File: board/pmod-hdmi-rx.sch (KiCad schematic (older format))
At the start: 15 parts, among them P1 PMOD-CONN_6X2, U31 XC9140, U32 REG710-DBV

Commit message: Rewriting for RX.
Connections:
- net HDMI_TX0_CLK+ renamed HDMI_RX0_CLK+
- net HDMI_TX0_CLK- renamed HDMI_RX0_CLK-
- net HDMI_TX0_D0+ renamed HDMI_RX0_D0+
- net HDMI_TX0_D0- renamed HDMI_RX0_D0-
- net HDMI_TX0_D1+ renamed HDMI_RX0_D1+
- net HDMI_TX0_D1- renamed HDMI_RX0_D1-
- net HDMI_TX0_D2+ renamed HDMI_RX0_D2+
- net HDMI_TX0_D2- renamed HDMI_RX0_D2-
- net HDMI_TX0_DCC_EN renamed HDMI_RX0_DCC_EN
- net HDMI_TX0_DDET renamed HDMI_RX0_DDET
- net HDMI_TX0_EQ0 renamed HDMI_RX0_EQ0
- net HDMI_TX0_EQ1 renamed HDMI_RX0_EQ1
- net TX05V0 renamed RX05V0
- net ~HDMI_TX0_OE renamed ~HDMI_RX0_OE
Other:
- note added: "On PRX0\n - DET on Pin X\n - DDC on Pin X\n - EQ1 on Pin X\n - EQ0 on Pin X"
- note added: "On PRX0\n - SCL on Pin X\n - SDA on Pin X\n - CEC on Pin X\n - HPD on Pin X"
- note removed: "On PTX0\n - DET on Pin X\n - DDC on Pin X\n - EQ1 on Pin X\n - EQ0 on Pin X"
- note removed: "On PTX0\n - SCL on Pin X\n - SDA on Pin X\n - CEC on Pin X\n - HPD on Pin X"
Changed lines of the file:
@@
 LIBS:xc9140
 LIBS:reg710-dbv
-LIBS:pmod-hdmi-tx-cache
+LIBS:pmod-hdmi-rx-cache
 EELAYER 25 0
 EELAYER END
@@
 Date ""
 Rev ""
-Comp "https://github.com/mithro/pmod-hdmi-tx-ptn3363"
-Comment1 "Using references from Numato Lab and Apertus AXIOM"
+Comp "https://github.com/mithro/pmod-hdmi-rx-ad8195"
+Comment1 ""
 Comment2 "Designed by TimVideos.us"
 Comment3 "License: CC-BY-SA 4.0 International"
@@
 S 4150 1400 2100 1600
 U 5802F547
-F0 "HDMI TX" 60
-F1 "hdmi_TX0.sch" 60
-F2 "~HDMI_TX0_OE" I R 6250 2000 60
-F3 "HDMI_TX0_EQ0" I R 6250 2600 60
-F4 "HDMI_TX0_EQ1" I R 6250 2500 60
-F5 "HDMI_TX0_DDC_EN" I R 6250 2350 60
-F6 "HDMI_TX0_CLK+" I L 4150 2250 60
-F7 "HDMI_TX0_CLK-" I L 4150 2350 60
-F8 "HDMI_TX0_D0+" I L 4150 2000 60
-F9 "HDMI_TX0_D0-" I L 4150 2100 60
-F10 "HDMI_TX0_D1+" I L 4150 1750 60
-F11 "HDMI_TX0_D1-" I L 4150 1850 60
-F12 "HDMI_TX0_D2+" I L 4150 1500 60
-F13 "HDMI_TX0_D2-" I L 4150 1600 60
-F14 "HDMI_TX0_SCL" B R 6250 1500 60
-F15 "HDMI_TX0_SDA" B R 6250 1600 60
-F16 "HDMI_TX0_DDET" I R 6250 2250 60
-F17 "HDMI_TX0_HPD" O R 6250 1800 60
-F18 "HDMI_TX0_HIZ_EN" I R 6250 2100 60
-F19 "HDMI_TX0_CEC" I R 6250 1700 60
+F0 "HDMI RX" 60
+F1 "hdmi_RX0.sch" 60
+F2 "~HDMI_RX0_OE" I R 6250 2000 60
+F3 "HDMI_RX0_EQ0" I R 6250 2600 60
+F4 "HDMI_RX0_EQ1" I R 6250 2500 60
+F5 "HDMI_RX0_DDC_EN" I R 6250 2350 60
+F6 "HDMI_RX0_CLK+" I L 4150 2250 60
+F7 "HDMI_RX0_CLK-" I L 4150 2350 60
+F8 "HDMI_RX0_D0+" I L 4150 2000 60
+F9 "HDMI_RX0_D0-" I L 4150 2100 60
+F10 "HDMI_RX0_D1+" I L 4150 1750 60
+F11 "HDMI_RX0_D1-" I L 4150 1850 60
+F12 "HDMI_RX0_D2+" I L 4150 1500 60
+F13 "HDMI_RX0_D2-" I L 4150 1600 60
+F14 "HDMI_RX0_SCL" B R 6250 1500 60
+F15 "HDMI_RX0_SDA" B R 6250 1600 60
+F16 "HDMI_RX0_DDET" I R 6250 2250 60
+F17 "HDMI_RX0_HPD" O R 6250 1800 60
+F18 "HDMI_RX0_HIZ_EN" I R 6250 2100 60
+F19 "HDMI_RX0_CEC" I R 6250 1700 60
 $EndSheet
 Text Label 3300 3000 0    60   ~ 0
-HDMI_TX0_CLK-
+HDMI_RX0_CLK-
 Text Label 3300 2900 0    60   ~ 0
-HDMI_TX0_D0-
+HDMI_RX0_D0-
 Text Label 3300 2800 0    60   ~ 0
-HDMI_TX0_D1-
+HDMI_RX0_D1-
 Text Label 3300 2700 0    60   ~ 0
-HDMI_TX0_D2-
+HDMI_RX0_D2-
 Text Label 1700 2700 2    60   ~ 0
-HDMI_TX0_D2+
+HDMI_RX0_D2+
 Text Label 1700 2800 2    60   ~ 0
-HDMI_TX0_D1+
+HDMI_RX0_D1+
 Text Label 1700 2900 2    60   ~ 0
-HDMI_TX0_D0+
+HDMI_RX0_D0+
 Text Label 1700 3000 2    60   ~ 0
-HDMI_TX0_CLK+
+HDMI_RX0_CLK+
 $Comp
 L GND #PWR01
@@
 $EndComp
 Text GLabel 3550 6000 2    60   Input ~ 0
-TX05V0
+RX05V0
 Text GLabel 5250 1125 2    60   Input ~ 0
 VCC3V3
 Text Label 3550 6075 3    60   ~ 0
-TX05V0
+RX05V0
 $Comp
 L GND #PWR05
@@
 Option 1\n
 Text Label 8125 1500 0    60   ~ 0
-HDMI_TX0_SCL
+HDMI_RX0_SCL
 Text Label 8125 1600 0    60   ~ 0
-HDMI_TX0_SDA
+HDMI_RX0_SDA
 Text Label 8125 1700 0    60   ~ 0
-HDMI_TX0_CEC
+HDMI_RX0_CEC
 Text Label 8125 1800 0    60   ~ 0
-HDMI_TX0_HPD
+HDMI_RX0_HPD
 Text Notes 8875 1850 0    60   ~ 0
-On PTX0\n - SCL on Pin X\n - SDA on Pin X\n - CEC on Pin X\n - HPD on Pin X
+On PRX0\n - SCL on Pin X\n - SDA on Pin X\n - CEC on Pin X\n - HPD on Pin X
 Text Notes 1850 4200 0    60   ~ 0
 HDMI High Speed Signals\nPositive signals on Top Row\nNegative signals on Bottom Row
@@
 $EndComp
 Text Label 7975 2500 0    60   ~ 0
-HDMI_TX0_EQ1
+HDMI_RX0_EQ1
 Text Label 7975 2600 0    60   ~ 0
-HDMI_TX0_EQ0
+HDMI_RX0_EQ0
 Text Notes 8875 2600 0    60   ~ 0
-On PTX0\n - DET on Pin X\n - DDC on Pin X\n - EQ1 on Pin X\n - EQ0 on Pin X
+On PRX0\n - DET on Pin X\n - DDC on Pin X\n - EQ1 on Pin X\n - EQ0 on Pin X
 Text Label 7975 2250 0    60   ~ 0
-HDMI_TX0_DDET
+HDMI_RX0_DDET
 Text Label 7975 2350 0    60   ~ 0
-HDMI_TX0_DCC_EN
+HDMI_RX0_DCC_EN
 Text Label 6300 2000 0    60   ~ 0
-~HDMI_TX0_OE
+~HDMI_RX0_OE
 Text Label 6300 2100 0    60   ~ 0
-HDMI_TX0_HIZ_EN
+HDMI_RX0_HIZ_EN
 $Comp
 L R RDE1

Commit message: Getting RX wired up.
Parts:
- removed ROE1: 10k, Resistors_SMD:R_0402, symbol R
- added D0, D1: LED, symbol LED
- added PE1: CONN_02X02, symbol CONN_02X02
- added PWP1: CONN_02X01, symbol CONN_02X01
- added RWP1: 10k, symbol R
- added UE1: 24AA01/24LC01B, symbol 24AA01/24LC01B
- RD0: renamed from REQ1; value 10k -> 100
- RD1: renamed from REQ0; value 10k -> 100
- renumbered RDC1 to RPE1, RDE1 to RTX1
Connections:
- net GND: now also RWP1.2, UE1.2 (VSS); no longer RPE1.1, RTX1.1
- net HDMI_RX0_SCL: now also PE1.1 (P1)
- net HDMI_RX0_SDA: now also PE1.3 (P3)
- net VCC: now also RPE1.1, RTX1.1, D0.2 (A), D1.2 (A), PWP1.2 (P2), UE1.4 (VCC); no longer RD0.1, RD1.1
- net HDMI_RX0_DCC_EN renamed HDMI_RX0_PEEN
- net HDMI_RX0_DDET renamed HDMI_RX0_TXEN
- net HDMI_RX0_EQ0 renamed HDMI_RX0_IO1
- net HDMI_RX0_EQ1 renamed HDMI_RX0_IO0
- net RX05V0 renamed VCC5V0
- new net: PWP1.1 (P1), RWP1.1, UE1.5 (WP)
- new net: D0.1 (K), RD0.1
- new net: D1.1 (K), RD1.1
- new net EEPROM_SCL: PE1.2 (P2), UE1.1 (SCL)
- new net EEPROM_SDA: PE1.4 (P4), UE1.3 (SDA)
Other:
- note added: "Jumpering PW1 will cause the \nEEPROM to be read only."
- note added: "On PRX0\n - TXEN on Pin X\n - PEEN on Pin X\n - IO0 on Pin X\n - IO1 on Pin X"
- note added: "TXEN is pulled high (1) by default, enabling receive.\nPEEN is pulled high (1) by default, enabling 6dB preemphasis."
- note removed: "By default, EQ0 and EQ1\nare pulled to VCC\ngiving 6dB equalization"
- note removed: "On PRX0\n - DET on Pin X\n - DDC on Pin X\n - EQ1 on Pin X\n - EQ0 on Pin X"

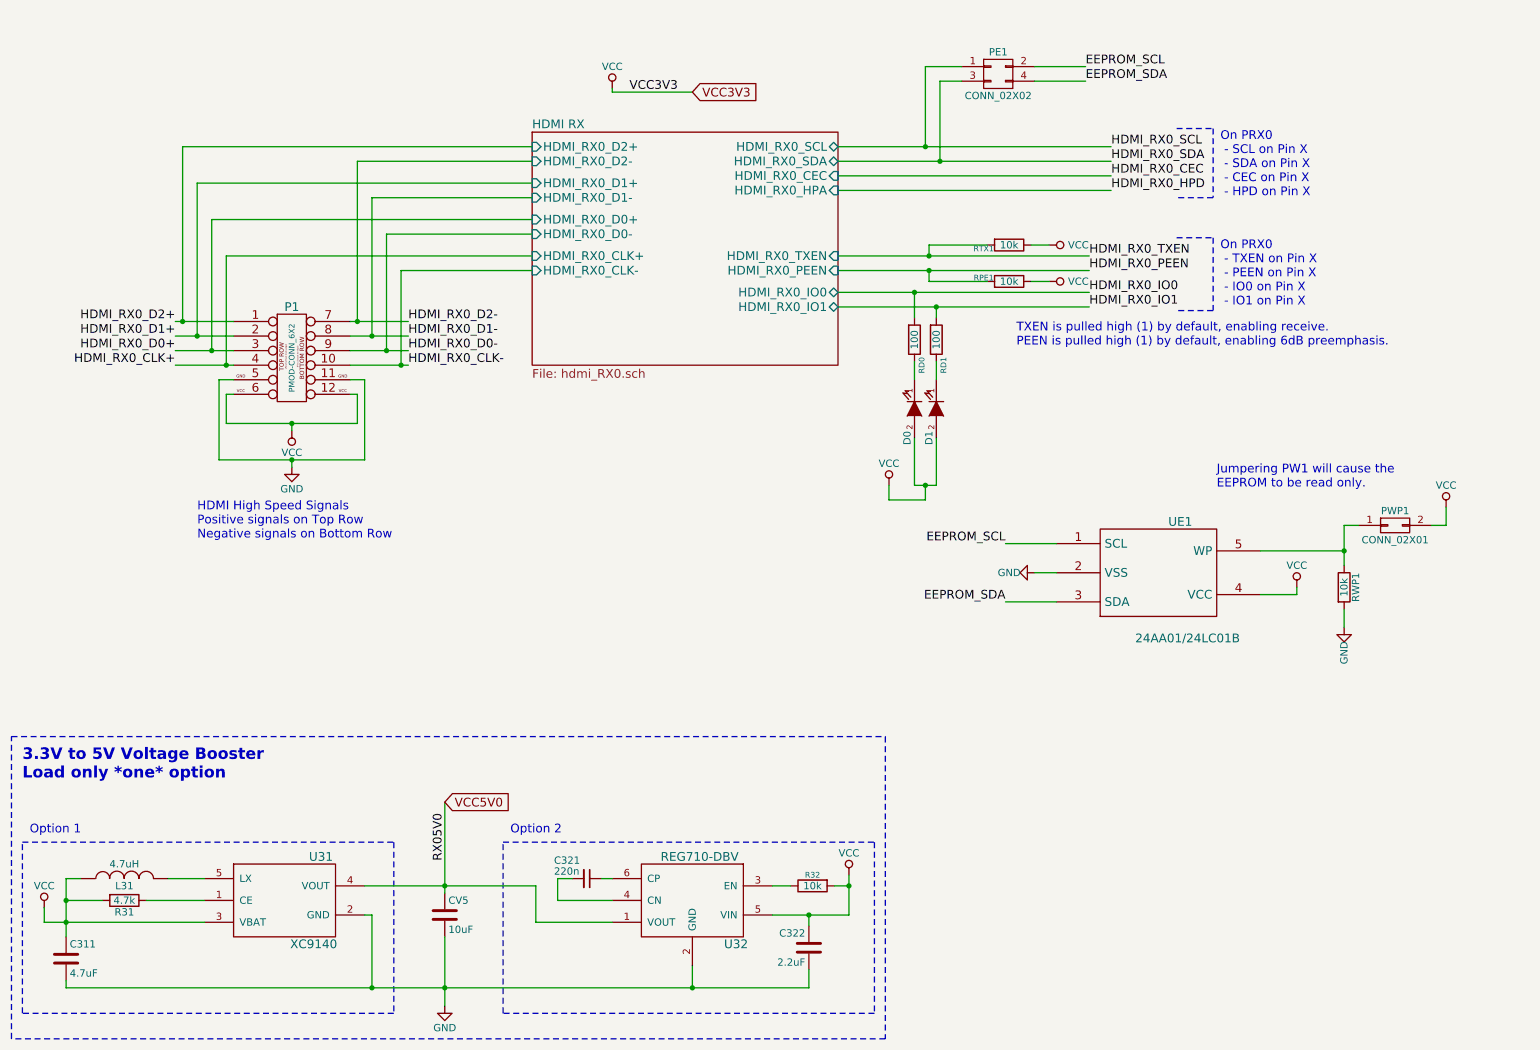
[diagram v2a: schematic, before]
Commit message: Slowly getting the RX version working.
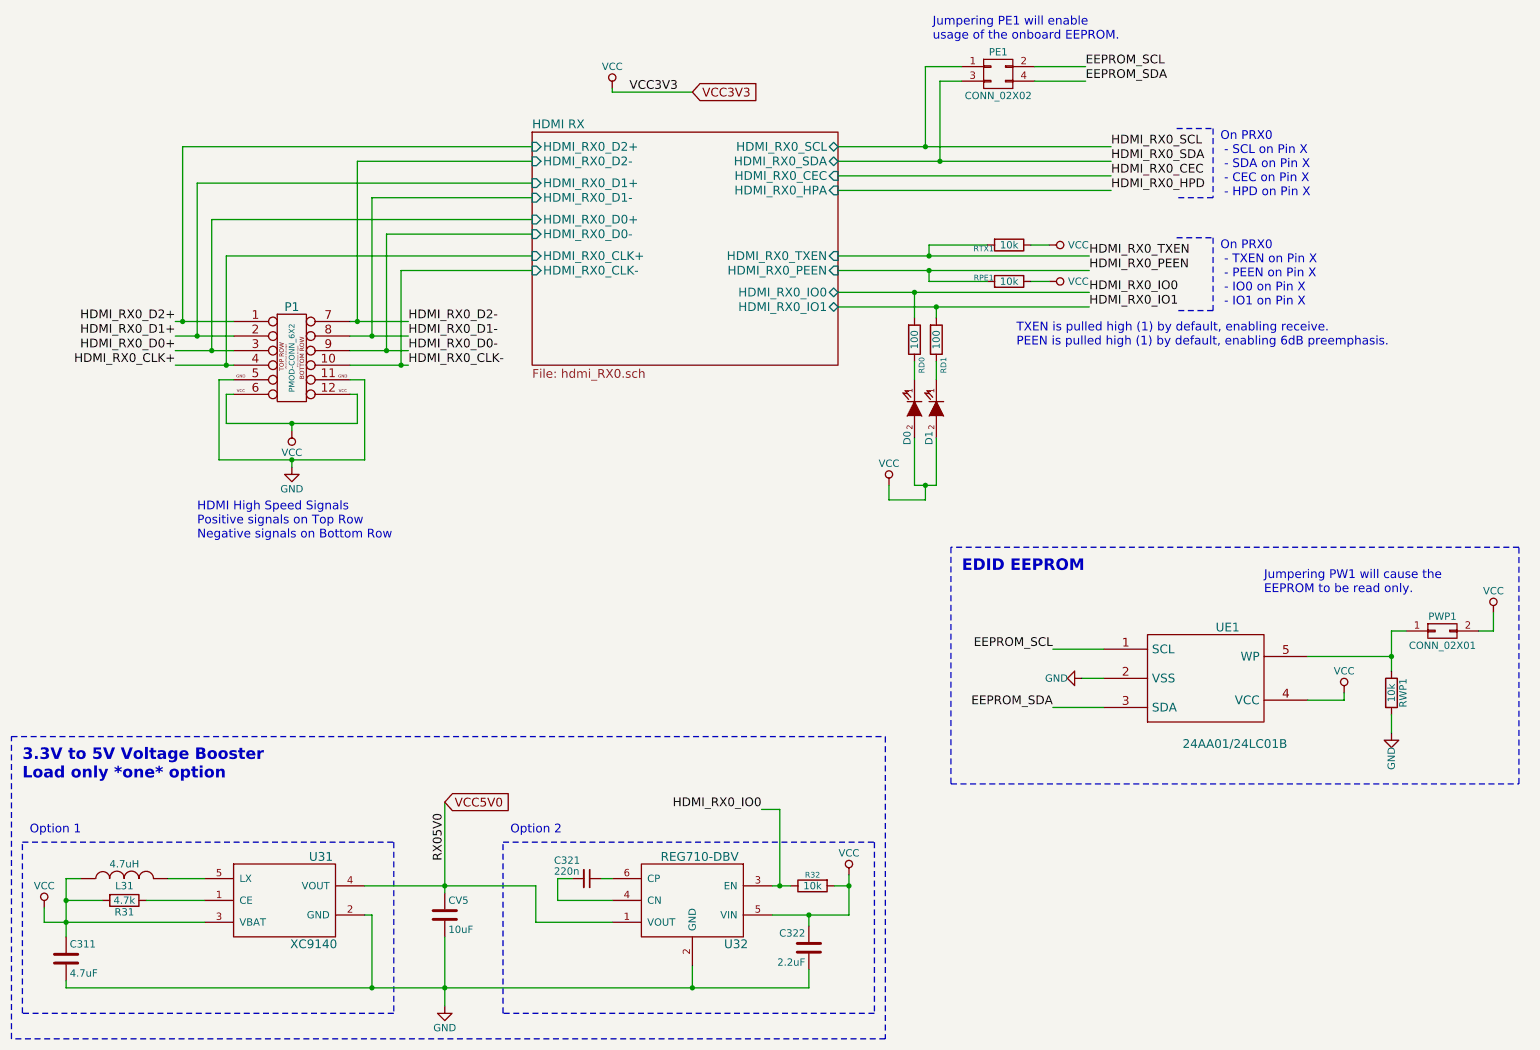
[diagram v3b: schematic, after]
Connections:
- net HDMI_RX0_IO0: now also R32.1, U32.3 (EN)
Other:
- note added: "EDID EEPROM"
- note added: "Jumpering PE1 will enable\nusage of the onboard EEPROM."
- moved on the sheet: PWP1, RWP1, UE1
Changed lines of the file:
@@
 LIBS:pmod
 LIBS:hdmi
-LIBS:ptn3363
 LIBS:ma78l00
 LIBS:pmod-conn_6x2
@@
 LIBS:xc9140
 LIBS:reg710-dbv
+LIBS:ad8195
+LIBS:fdv301n
 LIBS:pmod-hdmi-rx-cache
 EELAYER 25 0
@@
 L VCC #PWR08
 U 1 1 58039EF2
-P 9400 4525
-F 0 "#PWR08" H 9400 4375 50  0001 C CNN
-F 1 "VCC" H 9400 4675 50  0000 C CNN
-F 2 "" H 9400 4525 50  0000 C CNN
-F 3 "" H 9400 4525 50  0000 C CNN
-	1    9400 4525
+P 9725 5250
+F 0 "#PWR08" H 9725 5100 50  0001 C CNN
+F 1 "VCC" H 9725 5400 50  0000 C CNN
+F 2 "" H 9725 5250 50  0000 C CNN
+F 3 "" H 9725 5250 50  0000 C CNN
+	1    9725 5250
 	1    0    0    -1
 $EndComp
@@
 	2900 3100 3000 3100
 Wire Wire Line
-	3000 3650 3000 3100
-Wire Wire Line
-	2000 3650 3000 3650
+	3000 3100 3000 3650
+Wire Wire Line
+	3000 3650 2000 3650
 Wire Wire Line
 	2000 3650 2000 3100
@@
 L 24AA01/24LC01B UE1
 U 1 1 58037E0C
-P 8450 4425
-F 0 "UE1" H 8600 4775 60  0000 C CNN
-F 1 "24AA01/24LC01B" H 8650 3975 60  0000 C CNN
-F 2 "" H 8450 4425 60  0000 C CNN
-F 3 "" H 8450 4425 60  0000 C CNN
-	1    8450 4425
-	1    0    0    -1
-$EndComp
-Wire Wire Line
-	7750 4225 7400 4225
-Wire Wire Line
-	7750 4625 7400 4625
-Text Label 7400 4225 2    60   ~ 0
+P 8775 5150
+F 0 "UE1" H 8925 5500 60  0000 C CNN
+F 1 "24AA01/24LC01B" H 8975 4700 60  0000 C CNN
+F 2 "" H 8775 5150 60  0000 C CNN
+F 3 "" H 8775 5150 60  0000 C CNN
+	1    8775 5150
+	1    0    0    -1
+$EndComp
+Wire Wire Line
+	8075 4950 7725 4950
+Wire Wire Line
+	8075 5350 7725 5350
+Text Label 7725 4950 2    60   ~ 0
 EEPROM_SCL
-Text Label 7400 4625 2    60   ~ 0
+Text Label 7725 5350 2    60   ~ 0
 EEPROM_SDA
 $Comp
 L GND #PWR?
 U 1 1 5803B7CA
-P 7600 4425
-F 0 "#PWR?" H 7600 4175 50  0001 C CNN
-F 1 "GND" V 7600 4250 50  0000 C CNN
-F 2 "" H 7600 4425 50  0000 C CNN
-F 3 "" H 7600 4425 50  0000 C CNN
-	1    7600 4425
+P 7925 5150
+F 0 "#PWR?" H 7925 4900 50  0001 C CNN
+F 1 "GND" V 7925 4975 50  0000 C CNN
+F 2 "" H 7925 5150 50  0000 C CNN
+F 3 "" H 7925 5150 50  0000 C CNN
+	1    7925 5150
 	0    1    -1   0
 $EndComp
 Wire Wire Line
-	7750 4425 7600 4425
-Wire Wire Line
-	9400 4525 9400 4575
-Wire Wire Line
-	9400 4575 9150 4575
-Wire Wire Line
-	9150 4275 9725 4275
+	8075 5150 7925 5150
+Wire Wire Line
+	9725 5250 9725 5300
+Wire Wire Line
+	9725 5300 9475 5300
+Wire Wire Line
+	9475 5000 10050 5000
 $Comp
 L R RWP1
 U 1 1 5803C11E
-P 9725 4525
-F 0 "RWP1" V 9805 4525 50  0000 C CNN
-F 1 "10k" V 9725 4525 50  0000 C CNN
-F 2 "" V 9655 4525 50  0000 C CNN
-F 3 "" H 9725 4525 50  0000 C CNN
-	1    9725 4525
-	1    0    0    -1
-$EndComp
-Wire Wire Line
-	9725 4100 9725 4375
-Wire Wire Line
-	9725 4675 9725 4800
+P 10050 5250
+F 0 "RWP1" V 10130 5250 50  0000 C CNN
+F 1 "10k" V 10050 5250 50  0000 C CNN
+F 2 "" V 9980 5250 50  0000 C CNN
+F 3 "" H 10050 5250 50  0000 C CNN
+	1    10050 5250
+	1    0    0    -1
+$EndComp
+Wire Wire Line
+	10050 4825 10050 5100
+Wire Wire Line
+	10050 5400 10050 5525
 $Comp
 L GND #PWR?
 U 1 1 5803C747
-P 9725 4800
-F 0 "#PWR?" H 9725 4550 50  0001 C CNN
-F 1 "GND" V 9725 4625 50  0000 C CNN
-F 2 "" H 9725 4800 50  0000 C CNN
-F 3 "" H 9725 4800 50  0000 C CNN
-	1    9725 4800
+P 10050 5525
+F 0 "#PWR?" H 10050 5275 50  0001 C CNN
+F 1 "GND" V 10050 5350 50  0000 C CNN
+F 2 "" H 10050 5525 50  0000 C CNN
+F 3 "" H 10050 5525 50  0000 C CNN
+	1    10050 5525
 	-1   0    0    -1
 $EndComp
@@
 L CONN_02X01 PWP1
 U 1 1 5803C8DA
-P 10075 4100
-F 0 "PWP1" H 10075 4200 50  0000 C CNN
-F 1 "CONN_02X01" H 10075 4000 50  0000 C CNN
-F 2 "" H 10075 2900 50  0000 C CNN
-F 3 "" H 10075 2900 50  0000 C CNN
-	1    10075 4100
-	1    0    0    -1
-$EndComp
-Wire Wire Line
-	9725 4100 9825 4100
-Connection ~ 9725 4275
-Wire Wire Line
-	10325 4100 10425 4100
-Wire Wire Line
-	10425 4100 10425 3975
+P 10400 4825
+F 0 "PWP1" H 10400 4925 50  0000 C CNN
+F 1 "CONN_02X01" H 10400 4725 50  0000 C CNN
+F 2 "" H 10400 3625 50  0000 C CNN
+F 3 "" H 10400 3625 50  0000 C CNN
+	1    10400 4825
+	1    0    0    -1
+$EndComp
+Wire Wire Line
+	10050 4825 10150 4825
+Connection ~ 10050 5000
+Wire Wire Line
+	10650 4825 10750 4825
+Wire Wire Line
+	10750 4825 10750 4700
 $Comp
 L VCC #PWR?
 U 1 1 5803CDCA
-P 10425 3975
-F 0 "#PWR?" H 10425 3825 50  0001 C CNN
-F 1 "VCC" H 10425 4125 50  0000 C CNN
-F 2 "" H 10425 3975 50  0000 C CNN
-F 3 "" H 10425 3975 50  0000 C CNN
-	1    10425 3975
-	1    0    0    -1
-$EndComp
-Text Notes 8850 3850 0    60   ~ 0
+P 10750 4700
+F 0 "#PWR?" H 10750 4550 50  0001 C CNN
+F 1 "VCC" H 10750 4850 50  0000 C CNN
+F 2 "" H 10750 4700 50  0000 C CNN
+F 3 "" H 10750 4700 50  0000 C CNN
+	1    10750 4700
+	1    0    0    -1
+$EndComp
+Text Notes 9175 4575 0    60   ~ 0
 Jumpering PW1 will cause the \nEEPROM to be read only.
 $Comp
@@
 Text Notes 7475 2875 0    60   ~ 0
 TXEN is pulled high (1) by default, enabling receive.\nPEEN is pulled high (1) by default, enabling 6dB preemphasis.
+Wire Wire Line
+	5850 6575 5850 6050
+Connection ~ 5850 6575
+Wire Wire Line
+	5850 6050 5725 6050
+Text Label 5725 6050 2    60   ~ 0
+HDMI_RX0_IO0
+Text Notes 6900 775  0    60   ~ 0
+Jumpering PE1 will enable\nusage of the onboard EEPROM.
+Wire Notes Line
+	10925 4250 7025 4250
+Wire Notes Line
+	7025 4250 7025 5875
+Wire Notes Line
+	7025 5875 10925 5875
+Wire Notes Line
+	10925 5875 10925 4250
+Text Notes 7100 4425 0    79   ~ 16
+EDID EEPROM
 $EndSCHEMATC

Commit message: Adding footprints.
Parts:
- CV5: footprint Capacitors_SMD:C_1206 -> Capacitors_SMD:C_0603
- D0, D1: footprint (none) -> LEDs:LED_0603
- PE1: footprint (none) -> Pin_Headers:Pin_Header_Straight_2x02
- PWP1: footprint (none) -> Pin_Headers:Pin_Header_Straight_1x02
- RWP1: footprint (none) -> Resistors_SMD:R_0402
- UE1: footprint (none) -> TO_SOT_Packages_SMD:SOT-23-5
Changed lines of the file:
@@
 F 0 "CV5" H 3575 6875 50  0000 L CNN
 F 1 "10uF" H 3575 6675 50  0000 L CNN
-F 2 "Capacitors_SMD:C_1206" H 3588 6625 50  0001 C CNN
+F 2 "Capacitors_SMD:C_0603" H 3588 6625 50  0001 C CNN
 F 3 "" H 3550 6775 50  0000 C CNN
 	1    3550 6775
@@
 $EndComp
 $Comp
-L VCC #PWR08
+L VCC #PWR06
 U 1 1 58039EF2
 P 9725 5250
-F 0 "#PWR08" H 9725 5100 50  0001 C CNN
+F 0 "#PWR06" H 9725 5100 50  0001 C CNN
 F 1 "VCC" H 9725 5400 50  0000 C CNN
 F 2 "" H 9725 5250 50  0000 C CNN
@@
 $EndComp
 $Comp
-L VCC #PWR09
+L VCC #PWR07
 U 1 1 5803C0E2
 P 6325 6500
-F 0 "#PWR09" H 6325 6350 50  0001 C CNN
+F 0 "#PWR07" H 6325 6350 50  0001 C CNN
 F 1 "VCC" H 6325 6650 50  0000 C CNN
 F 2 "" H 6325 6500 50  0000 C CNN
@@
 F 0 "PE1" H 7350 1150 50  0000 C CNN
 F 1 "CONN_02X02" H 7350 850 50  0000 C CNN
-F 2 "" H 7350 -200 50  0000 C CNN
+F 2 "Pin_Headers:Pin_Header_Straight_2x02" H 7350 -200 50  0001 C CNN
 F 3 "" H 7350 -200 50  0000 C CNN
 	1    7350 1000
@@
 F 0 "UE1" H 8925 5500 60  0000 C CNN
 F 1 "24AA01/24LC01B" H 8975 4700 60  0000 C CNN
-F 2 "" H 8775 5150 60  0000 C CNN
+F 2 "TO_SOT_Packages_SMD:SOT-23-5" H 8775 5150 60  0001 C CNN
 F 3 "" H 8775 5150 60  0000 C CNN
 	1    8775 5150
@@
 EEPROM_SDA
 $Comp
-L GND #PWR?
+L GND #PWR08
 U 1 1 5803B7CA
 P 7925 5150
-F 0 "#PWR?" H 7925 4900 50  0001 C CNN
+F 0 "#PWR08" H 7925 4900 50  0001 C CNN
 F 1 "GND" V 7925 4975 50  0000 C CNN
 F 2 "" H 7925 5150 50  0000 C CNN
@@
 F 0 "RWP1" V 10130 5250 50  0000 C CNN
 F 1 "10k" V 10050 5250 50  0000 C CNN
-F 2 "" V 9980 5250 50  0000 C CNN
+F 2 "Resistors_SMD:R_0402" V 9980 5250 50  0001 C CNN
 F 3 "" H 10050 5250 50  0000 C CNN
 	1    10050 5250
@@
 	10050 5400 10050 5525
 $Comp
-L GND #PWR?
+L GND #PWR09
 U 1 1 5803C747
 P 10050 5525
-F 0 "#PWR?" H 10050 5275 50  0001 C CNN
+F 0 "#PWR09" H 10050 5275 50  0001 C CNN
 F 1 "GND" V 10050 5350 50  0000 C CNN
 F 2 "" H 10050 5525 50  0000 C CNN
@@
 F 0 "PWP1" H 10400 4925 50  0000 C CNN
 F 1 "CONN_02X01" H 10400 4725 50  0000 C CNN
-F 2 "" H 10400 3625 50  0000 C CNN
+F 2 "Pin_Headers:Pin_Header_Straight_1x02" H 10400 3625 50  0001 C CNN
 F 3 "" H 10400 3625 50  0000 C CNN
 	1    10400 4825
@@
 	10750 4825 10750 4700
 $Comp
-L VCC #PWR?
+L VCC #PWR010
 U 1 1 5803CDCA
 P 10750 4700
-F 0 "#PWR?" H 10750 4550 50  0001 C CNN
+F 0 "#PWR010" H 10750 4550 50  0001 C CNN
 F 1 "VCC" H 10750 4850 50  0000 C CNN
 F 2 "" H 10750 4700 50  0000 C CNN
@@
 Jumpering PW1 will cause the \nEEPROM to be read only.
 $Comp
-L VCC #PWR?
+L VCC #PWR011
 U 1 1 5803D45D
 P 6600 3825
-F 0 "#PWR?" H 6600 3675 50  0001 C CNN
+F 0 "#PWR011" H 6600 3675 50  0001 C CNN
 F 1 "VCC" H 6600 3975 50  0000 C CNN
 F 2 "" H 6600 3825 50  0000 C CNN
@@
 F 0 "D0" H 6975 3250 50  0000 C CNN
 F 1 "LED" H 6775 3200 50  0001 C CNN
-F 2 "" H 6775 3300 50  0000 C CNN
+F 2 "LEDs:LED_0603" H 6775 3300 50  0001 C CNN
 F 3 "" H 6775 3300 50  0000 C CNN
 	1    6775 3300
@@
 F 0 "D1" H 7125 3250 50  0000 C CNN
 F 1 "LED" H 6925 3200 50  0001 C CNN
-F 2 "" H 6925 3300 50  0000 C CNN
+F 2 "LEDs:LED_0603" H 6925 3300 50  0001 C CNN
 F 3 "" H 6925 3300 50  0000 C CNN
 	1    6925 3300
@@
 	6925 3100 6925 2975
 $Comp
-L VCC #PWR?
+L VCC #PWR012
 U 1 1 5803F3D1
 P 7700 2425
-F 0 "#PWR?" H 7700 2275 50  0001 C CNN
+F 0 "#PWR012" H 7700 2275 50  0001 C CNN
 F 1 "VCC" V 7700 2625 50  0000 C CNN
 F 2 "" H 7700 2425 50  0000 C CNN
@@
 $EndComp
 $Comp
-L VCC #PWR?
+L VCC #PWR013
 U 1 1 5803F7DD
 P 7700 2175
-F 0 "#PWR?" H 7700 2025 50  0001 C CNN
+F 0 "#PWR013" H 7700 2025 50  0001 C CNN
 F 1 "VCC" V 7700 2375 50  0000 C CNN
 F 2 "" H 7700 2175 50  0000 C CNN
